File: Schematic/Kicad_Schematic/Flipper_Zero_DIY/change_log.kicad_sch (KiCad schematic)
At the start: 0 parts

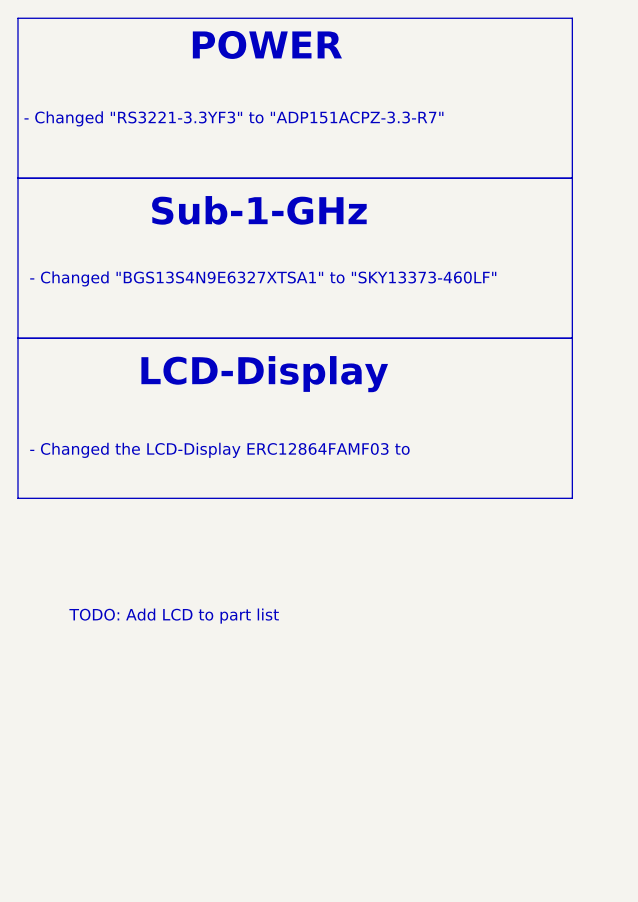
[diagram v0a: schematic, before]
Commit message: finished NFC_RFID-Blockdia and NFC Schematic
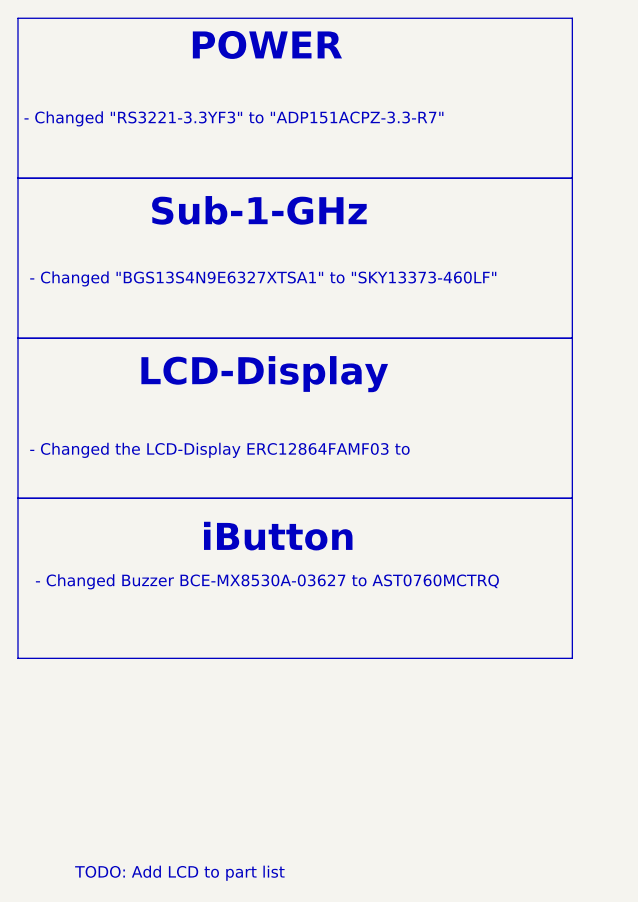
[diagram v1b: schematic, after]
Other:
- note added: "- Changed Buzzer BCE-MX8530A-03627 to AST0760MCTRQ"
- note added: "iButton"
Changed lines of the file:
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@@
+    (fill (type color) (color 226 255 40 0.57))
+  )
+  (rectangle (start 12.065 65.405) (end 73.66 83.185)
+    (stroke (width 0) (type default))
     (fill (type color) (color 226 255 40 0.57))
   )
@@
     (effects (font (size 3 3) (thickness 0.6) bold) (justify left bottom))
   )
-  (text "TODO: Add LCD to part list" (at 17.78 79.375 0)
+  (text "- Changed Buzzer BCE-MX8530A-03627 to AST0760MCTRQ"
+    (at 13.97 75.565 0)
+    (effects (font (size 1.27 1.27)) (justify left bottom))
+  )
+  (text "TODO: Add LCD to part list" (at 18.415 107.95 0)
     (effects (font (size 1.27 1.27)) (justify left bottom))
   )
@@
     (effects (font (size 3 3) bold) (justify left bottom))
   )
+  (text "iButton" (at 32.385 71.755 0)
+    (effects (font (size 3 3) (thickness 0.6) bold) (justify left bottom))
+  )
 )
